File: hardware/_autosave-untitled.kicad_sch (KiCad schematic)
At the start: 38 parts, among them IC1 ESP32-S3-WROOM-1-N8R8, J5 DCJ200-10-A-K1-K, J6 USB4105-GF-A, SW1 SW_Push, SW2 SW_Push, U3 NCP1117ST33T3G, U4 USBLC6-2SC6

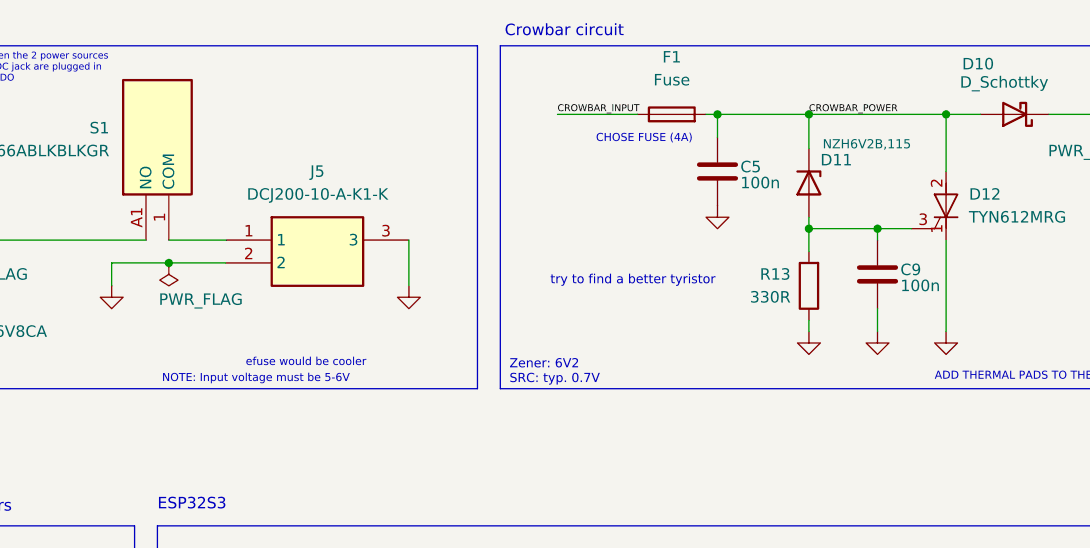
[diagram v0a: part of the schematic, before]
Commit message: Schematics adjustments - updated some components
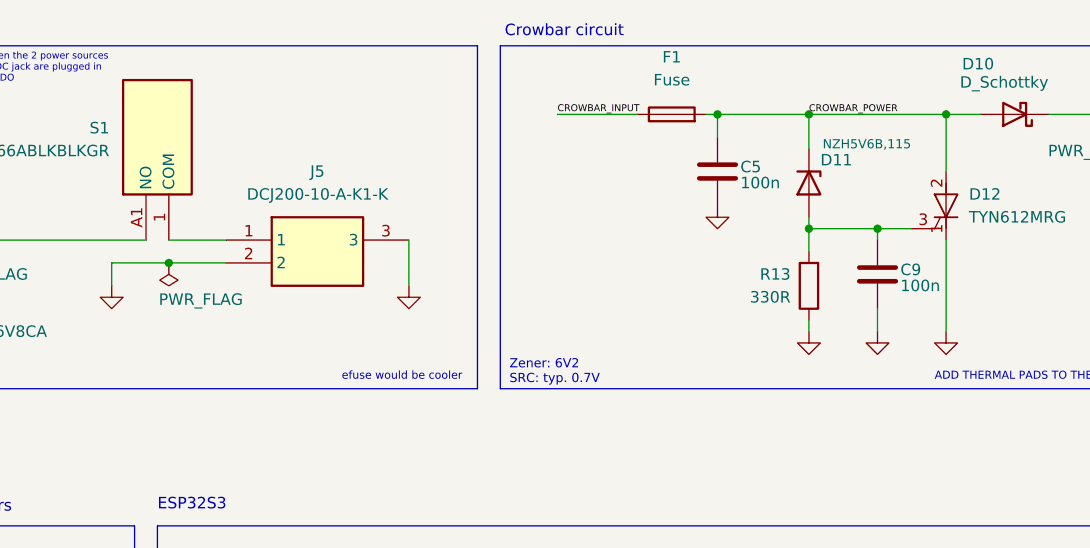
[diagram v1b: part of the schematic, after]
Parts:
- D11: value NZH6V2B,115 -> NZH5V6B,115
- D12: footprint ESP32-project-footprints:TO255P460X1020X2005-3P -> ESP32-project-footprints:TS820600B
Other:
- note removed: "CHOSE FUSE (4A)"
- note removed: "NOTE: Input voltage must be 5-6V"
- note removed: "try to find a better tyristor"
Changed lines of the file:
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@@
 		)
 	)
-	(text "CHOSE FUSE (4A)"
-		(exclude_from_sim no)
-		(at 219.202 30.734 0)
-		(effects
-			(font
-				(size 0.889 0.889)
-				(color 255 0 6 1)
-			)
-		)
-	)
 	(text "ADD THERMAL PADS TO THE SCR"
 		(exclude_from_sim no)
@@
 		)
 	)
-	(text "NOTE: Input voltage must be 5-6V"
-		(exclude_from_sim no)
-		(at 165.608 57.404 0)
-		(effects
-			(font
-				(size 0.889 0.889)
-				(color 255 4 0 1)
-			)
-			(justify left)
-		)
-	)
 	(text "50R"
 		(exclude_from_sim no)
@@
 	(text "efuse would be cooler"
 		(exclude_from_sim no)
-		(at 181.61 55.626 0)
+		(at 192.278 57.15 0)
 		(effects
 			(font
@@
 		)
 	)
-	(text "try to find a better tyristor"
-		(exclude_from_sim no)
-		(at 217.932 46.482 0)
-		(effects
-			(font
-				(size 1.016 1.016)
-				(color 255 0 0 1)
-			)
-		)
-	)
 	(text "ESP32S3"
 		(exclude_from_sim no)
@@
 			)
 		)
-		(property "Value" "NZH6V2B,115"
+		(property "Value" "NZH5V6B,115"
 			(at 239.014 31.242 90)
 			(effects
@@
 			)
 		)
-		(property "Description" "https://www.tme.eu/cz/details/nzh6v2b.115/zenerovy-diody-smd/nexperia/nzh6v2b-115/"
+		(property "Description" "https://www.tme.eu/cz/details/nzh5v6b.115/zenerovy-diody-smd/nexperia/nzh5v6b-115/"
 			(at 237.49 35.56 0)
 			(effects
@@
 			)
 		)
-		(property "Datasheet" "~"
+		(property "Datasheet" "https://www.tme.eu/cz/details/0679h3000-05/pojistky-smd-2410-rychle/bel-fuse/"
 			(at 222.25 27.94 0)
 			(effects
@@
 			)
 		)
-		(property "Footprint" "ESP32-project-footprints:TO255P460X1020X2005-3P"
+		(property "Footprint" "ESP32-project-footprints:TS820600B"
 			(at 252.73 38.1 90)
 			(effects
@@
 			)
 		)
-		(property "Datasheet" "https://www.tme.eu/Document/d9f9d794eaaafeac8e57e572c3e994db/TYN612M.pdf"
+		(property "Datasheet" "https://www.tme.eu/Document/912e5f9b8296aac23d7a6d68608ab042/TS820.pdf"
 			(at 252.73 38.1 90)
 			(effects
@@
 			)
 		)
-		(property "Description" "https://www.tme.eu/cz/details/tyn612mrg/tyristory-smd-tht/stmicroelectronics/"
+		(property "Description" "https://www.tme.eu/cz/details/ts820-600b/tyristory-smd-tht/stmicroelectronics/"
 			(at 252.73 38.1 0)
 			(effects
